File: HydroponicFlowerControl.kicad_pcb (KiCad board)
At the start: 4 copper layers, 101 x 101 mm, 236 parts, among them IC1 ADM3260ARSZ-RL7, IC2 ADM3260ARSZ-RL7, IC3 CH224K, J1 EC, J10 Pump 1, J11 Temperature, J12 Pump 2, J13 Pump 3, J14 D IN1, J15 D IN2, J16 D IN3, J17 CAN, J18 Raspberry_Pi_2_3, J19 Conn_ARM_JTAG_SWD_10, J2 Temp, J20 Conn_ARM_JTAG_SWD_10, J3 Flow, J4 pH, J5 USB_C_Receptacle_USB2.0, J6 Barrel_Jack, J7 Valve 1, J8 Valve 2, J9 Valve 3, Q1 MMBT3904, Q10 AO3401A, Q11 MMBT3904, Q12 AO3401A, Q2 AO3401A, Q3 MMBT3904, Q4 AO3401A, Q5 MMBT3904, Q6 AO3401A, Q7 MMBT3904, Q8 MMBT3904, Q9 AO3401A, SW1 RESET, U1 AT24C256C, U10 REF3020, U11 TPS60400DBV, U12 ADS1115IDGS, U14 TLV271, U15 TLV271, U16 MCP2518FD-xQBB, U17 HDC1080, U18 SN65HVD230, U19 SN65HVD230, U2 ADS1115IDGS, U20 TPS5430DDA, U4 TPS60400DBV, U5 LM324, U6 MCP4017T-502E/LT, U7 LM358, U8 STM32G431CBTx, U9 AMS1117-3.3, Y1 8 MHz, Y2 40MHz

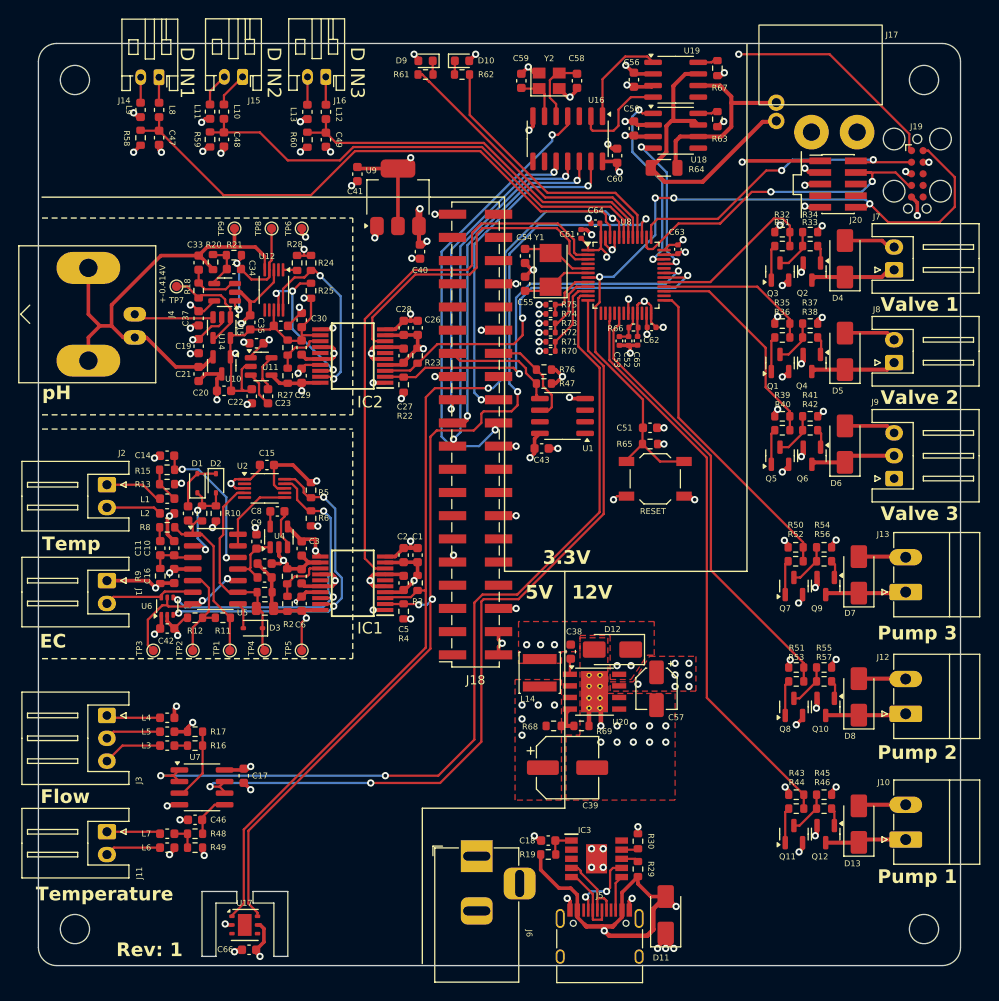
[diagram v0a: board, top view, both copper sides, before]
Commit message: Add testpoints for power and gnd
Closes #3
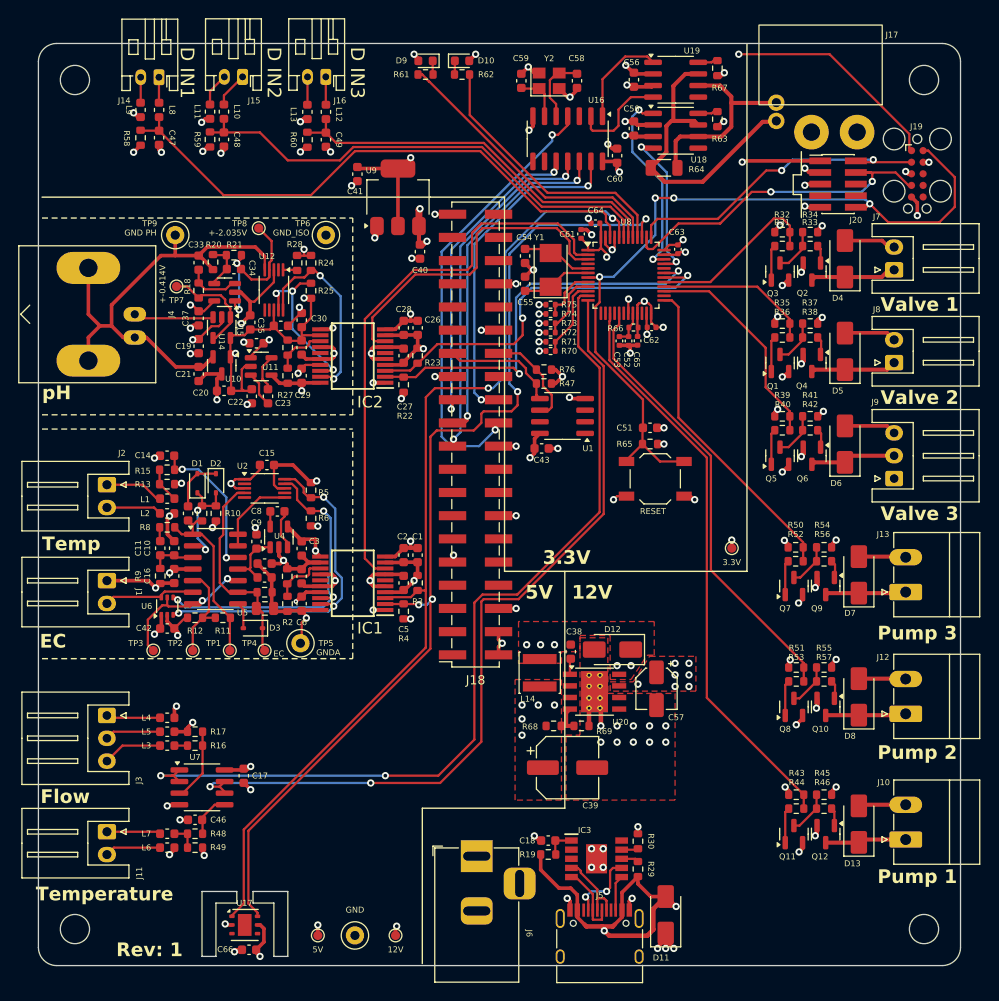
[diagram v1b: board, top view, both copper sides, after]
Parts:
- added TP10: 5V, TestPoint:TestPoint_Pad_D1.0mm, F.Cu at (88.6, 159.7)
- added TP11: 12V, TestPoint:TestPoint_Pad_D1.0mm, F.Cu at (97.1, 159.7)
- added TP12: 3.3V, TestPoint:TestPoint_Pad_D1.0mm, F.Cu at (133.9, 117.3)
- added TP13: GND, TestPoint:TestPoint_Loop_D1.80mm_Drill1.0mm_Beaded, F.Cu at (92.7, 159.7)
- TP4: value TestPoint_Small -> EC
- TP5: value GND_ISO -> GNDA; footprint TestPoint:TestPoint_Pad_D1.0mm -> TestPoint:TestPoint_Loop_D1.80mm_Drill1.0mm_Beaded
- TP6, TP9: footprint TestPoint:TestPoint_Pad_D1.0mm -> TestPoint:TestPoint_Loop_D1.80mm_Drill1.0mm_Beaded
- moved TP9 6.53 mm to (73.0, 83.0)
- moved TP6 2.75 mm to (89.5, 83.0)
- moved TP8 1.41 mm to (82.1, 82.2)
- moved TP5 0.81 mm to (86.7, 127.7)
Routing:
- net +12V: track 16.9 -> 30.5 mm, vias 22 -> 23
- net +5V: track 36.5 -> 37.7 mm, vias 16 -> 17
- net +3.3V: track 84.6 -> 85.5 mm, vias 21 -> 22
- net GND_iosPH: track 36.8 -> 36.0 mm, vias 11 -> 10
- net GNDA: track 51.8 -> 51.1 mm
- net /pH/PH_OUT: track 17.4 -> 18.0 mm

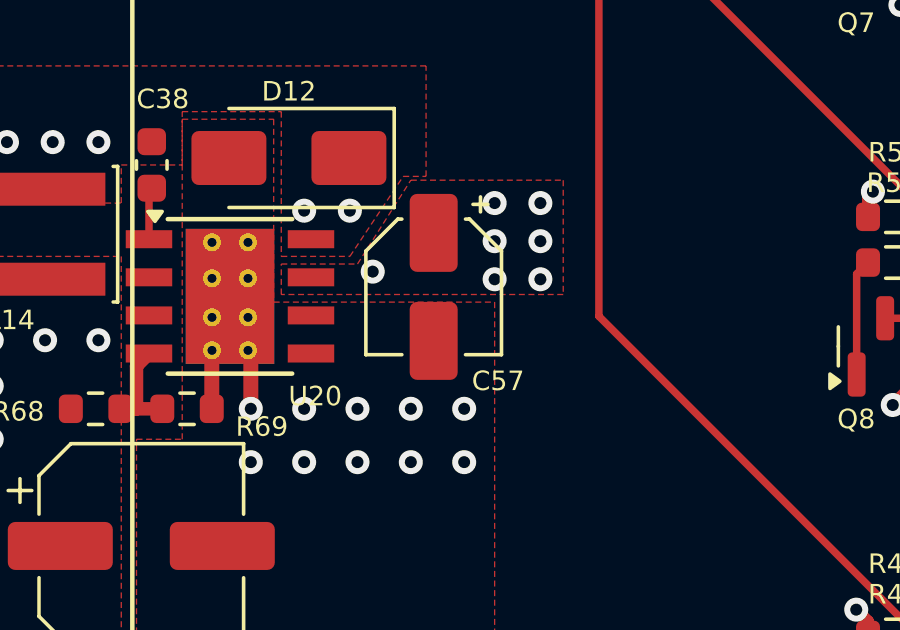
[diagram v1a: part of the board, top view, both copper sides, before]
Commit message: Replace C57
With a variant that can be used with economy pcbs at JLCPCB
Closes #25
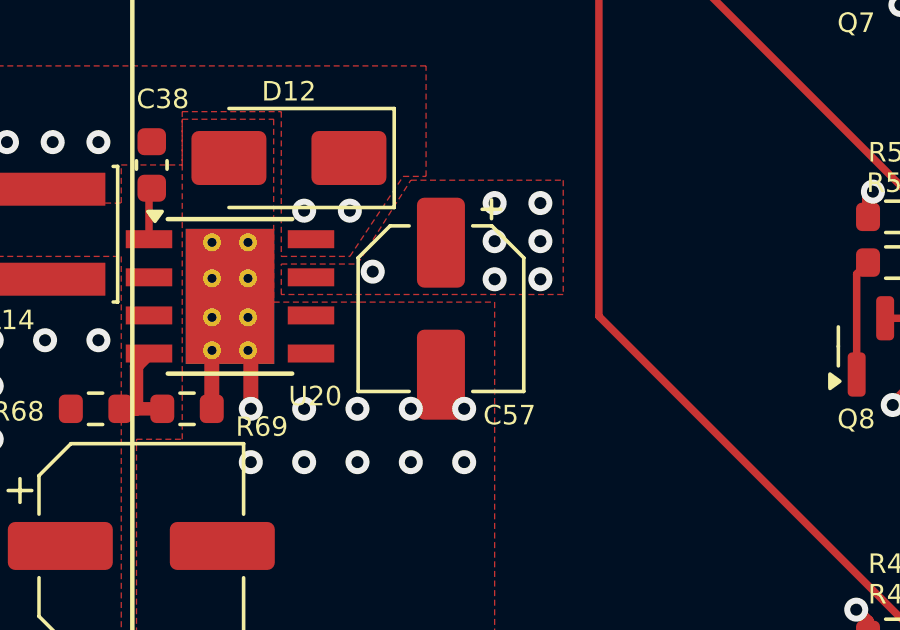
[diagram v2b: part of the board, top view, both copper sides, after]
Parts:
- C57: footprint Capacitor_SMD:CP_Elec_4x5.4 -> Capacitor_SMD:CP_Elec_5x5.4
- moved C57 0.77 mm to (125.9, 133.4)

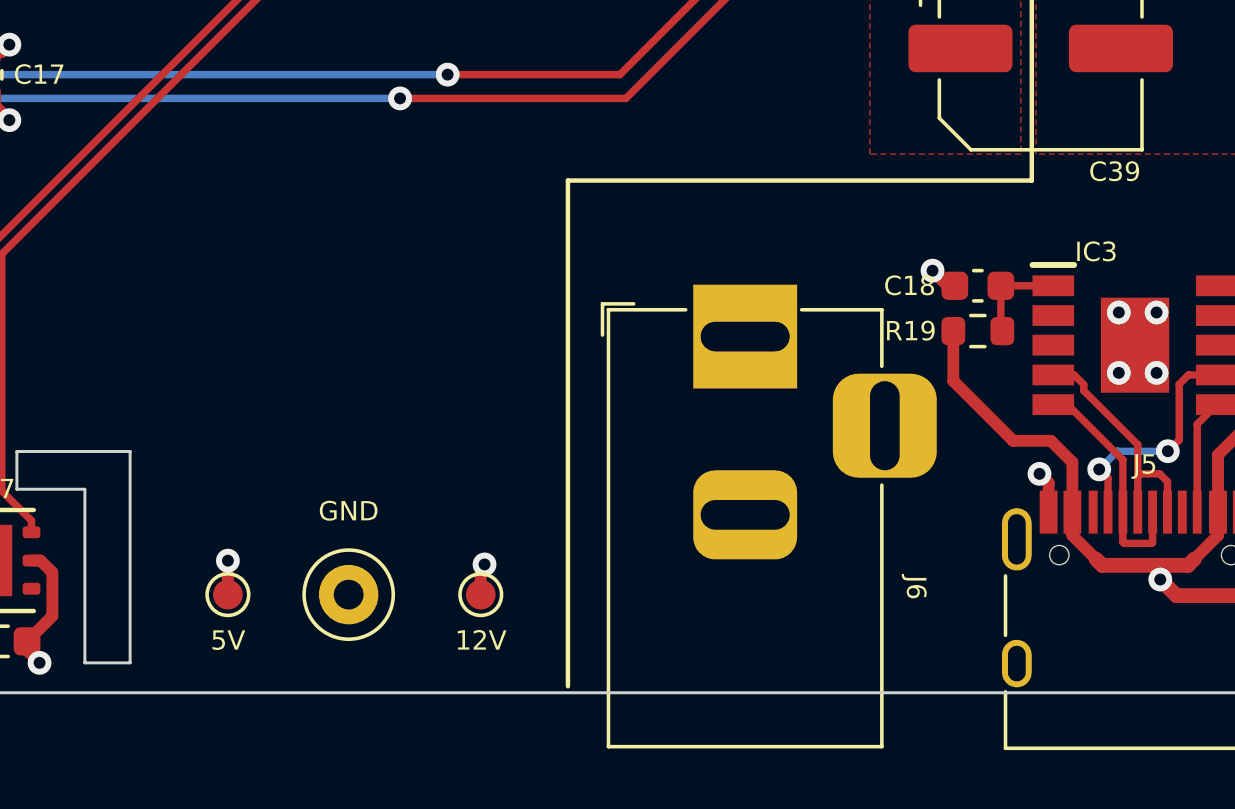
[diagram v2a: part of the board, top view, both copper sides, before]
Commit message: Replace DC connector with SMD variant
Closes #23
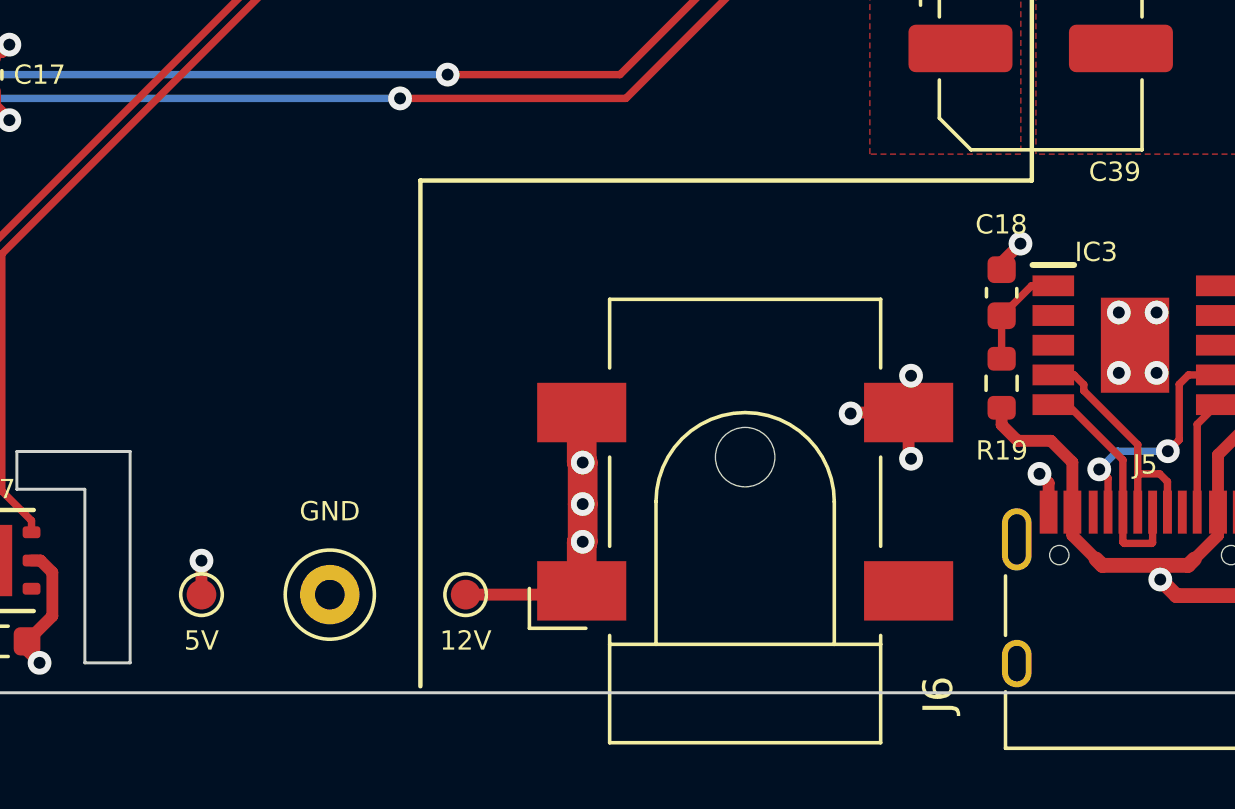
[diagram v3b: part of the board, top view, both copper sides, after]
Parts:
- J6: footprint Connector_BarrelJack:BarrelJack_Horizontal -> Connector_BarrelJack:BarrelJack_CLIFF_FC681465S_SMT_Horizontal
- moved J6 5.56 mm to (106.0, 156.6)
- moved R19 1.93 mm to (114.6, 152.6), turned to -90 degrees
- moved TP10 0.89 mm to (87.7, 159.7)
- moved C18 0.83 mm to (114.6, 149.5), turned to 90 degrees
- moved TP13 0.64 mm to (92.0, 159.7)
- moved TP11 0.51 mm to (96.6, 159.7)
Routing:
- net GND: track 154.4 -> 159.7 mm, vias 90 -> 93
- net +12V: track 30.5 -> 26.7 mm, vias 23 -> 25
- net VBUS: track 45.9 -> 42.6 mm

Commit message: Replace the mcu to a STM32G473 variant
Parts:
- U8: value STM32G431CBTx -> STM32G473CBTx
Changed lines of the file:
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@@
 			)
 		)
-		(property "Value" "STM32G431CBTx"
+		(property "Value" "STM32G473CBTx"
 			(at 0 5.85 0)
 			(layer "F.Fab")
@@
 			)
 		)
-		(property "Datasheet" "https://www.st.com/resource/en/datasheet/stm32g431cb.pdf"
+		(property "Datasheet" "https://www.st.com/resource/en/datasheet/stm32g473cb.pdf"
 			(at 0 0 0)
 			(unlocked yes)
@@
 			)
 		)
-		(property "Description" "STMicroelectronics Arm Cortex-M4 MCU, 128KB flash, 32KB RAM, 170 MHz, 1.71-3.6V, 38 GPIO, LQFP48"
+		(property "Description" "STMicroelectronics Arm Cortex-M4 MCU, 128KB flash, 128KB RAM, 170 MHz, 1.71-3.6V, 38 GPIO, LQFP48"
 			(at 0 0 0)
 			(unlocked yes)
@@
 			)
 		)
-		(property "LCSC" "C529355"
+		(property "LCSC" "C730111"
 			(at 0 0 0)
 			(unlocked yes)
-			(layer "F.Fab")
-			(hide yes)
-			(effects
-				(font
-					(size 1 1)
-					(thickness 0.15)
-				)
-			)
-		)
-		(property "LCSC alt" ""
-			(at 0 0 0)
-			(unlocked yes)

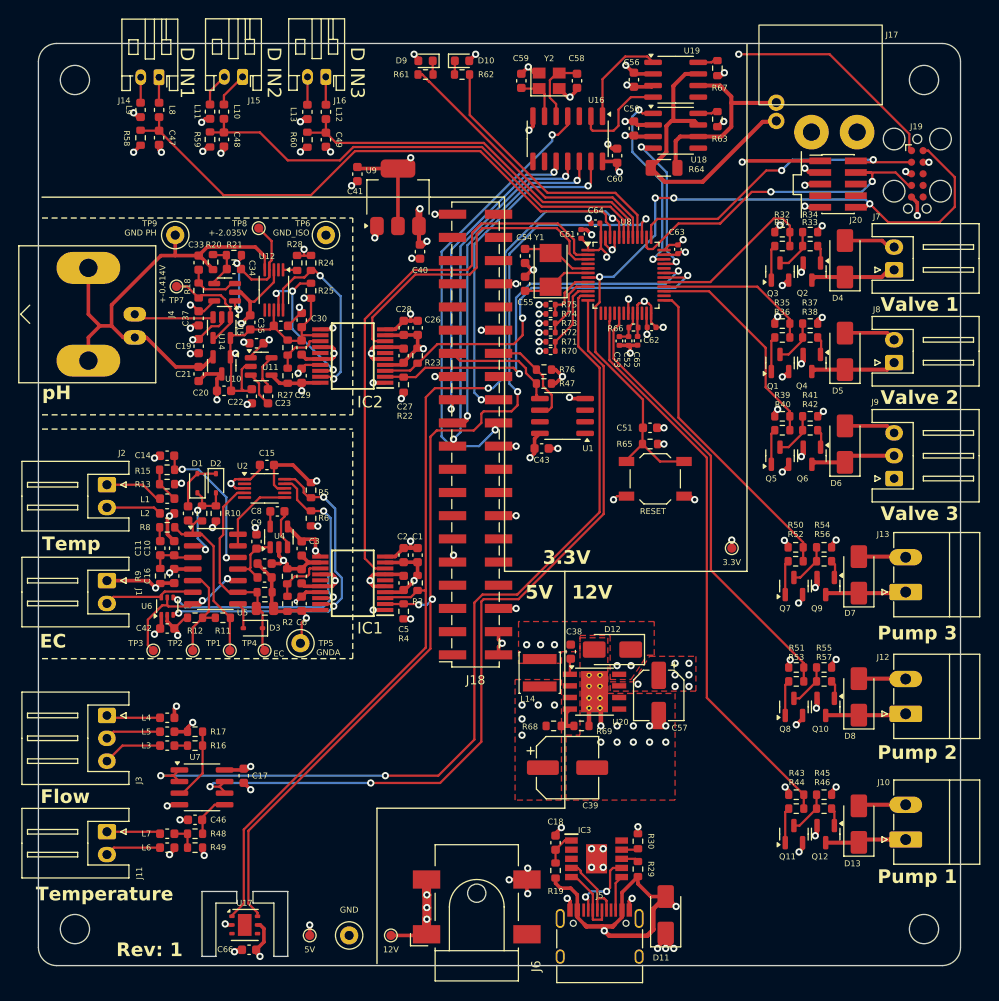
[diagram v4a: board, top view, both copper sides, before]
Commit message: Route USB data signals to STM32
The CANbus needed to be moved together with ec and ph disable signals.
Closes #14 and #9
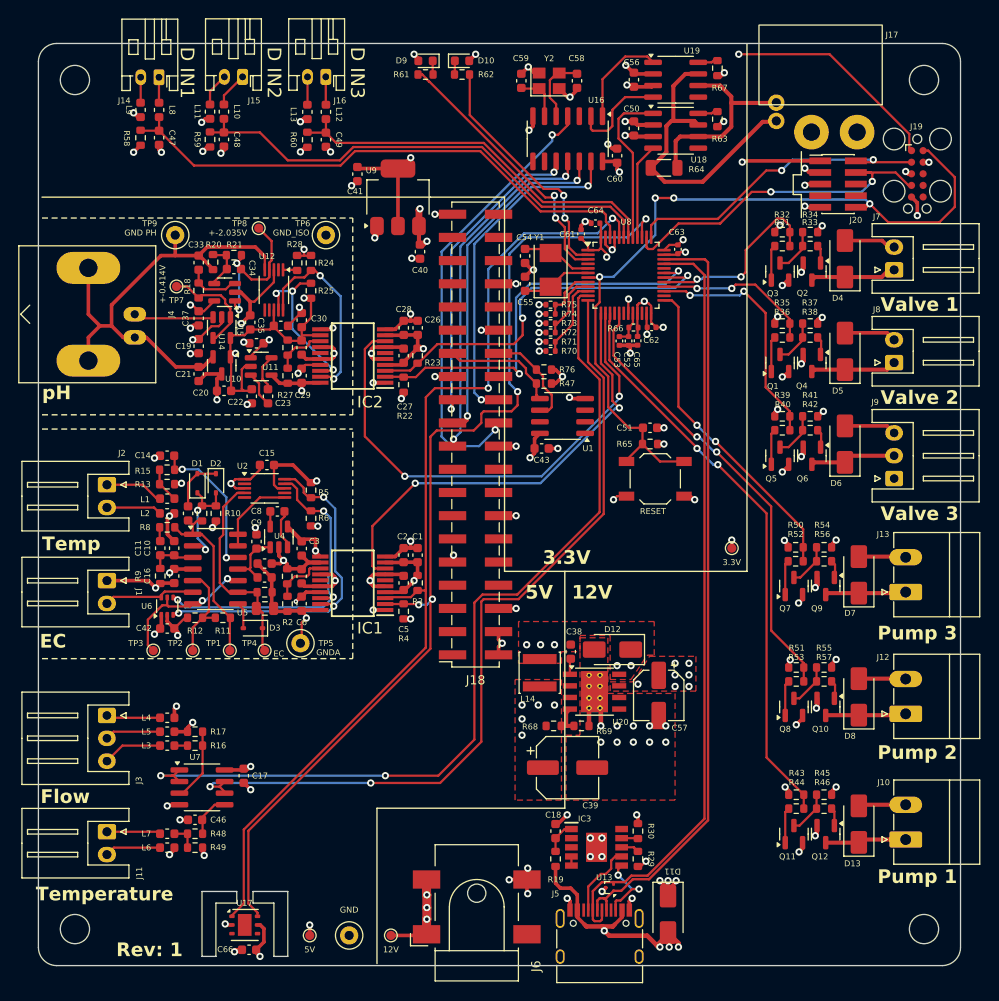
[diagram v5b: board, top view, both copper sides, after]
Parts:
- added U13: TPD2EUSB30, Package_TO_SOT_SMD:Texas_DRT-3, F.Cu at (120.6, 154.5)
- moved C18 1.27 mm to (114.6, 148.3)
- moved R19 1.27 mm to (114.6, 151.3)
- moved IC3 1.26 mm to (119.1, 150.0)
- moved R29 1.11 mm to (123.7, 151.3)
- moved R30 1.11 mm to (123.7, 148.3)
- moved D11 0.26 mm to (127.0, 157.4), turned to -90 degrees
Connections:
- IC3 pad 4: Net-(IC3-DP) -> Net-(IC3-DM)
- J5 pad A6: Net-(IC3-DP) -> /Power/USB_D+
- J5 pad A7: Net-(IC3-DM) -> /Power/USB_D-
- J5 pad B6: Net-(IC3-DP) -> /Power/USB_D+
- J5 pad B7: Net-(IC3-DM) -> /Power/USB_D-
- U8 pad 13: unconnected-(U8-PA5-Pad13) -> /EC/DISABLE
- U8 pad 14: unconnected-(U8-PA6-Pad14) -> /MCU/pH_disable
- U8 pad 2: /EC/DISABLE -> LED_CAN
- U8 pad 3: /MCU/pH_disable -> LED_HB
- U8 pad 33: CAN_RXD -> /Power/USB_D-
- U8 pad 34: CAN_TXD -> /Power/USB_D+
- U8 pad 40: LED_CAN -> CAN_RXD
- U8 pad 41: LED_HB -> CAN_TXD
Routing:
- net /Power/USB_D-: track 0.00 -> 85.5 mm
- net /Power/USB_D+: track 0.00 -> 84.3 mm
- net /MCU/pH_disable: track 35.9 -> 55.3 mm, vias 0 -> 2
- net /EC/DISABLE: track 62.0 -> 49.5 mm, vias 0 -> 2
- net Net-(IC3-DP): track 8.34 -> 0.00 mm
- net Net-(IC3-DM): track 7.45 -> 1.00 mm
- net CAN_RXD: track 16.7 -> 10.5 mm, vias 2 -> 0
- net /Power/CC2: track 3.89 -> 8.21 mm, vias 0 -> 2
- net VBUS: track 42.6 -> 46.7 mm, vias 2 -> 5
- net CAN_TXD: track 21.3 -> 17.7 mm, vias 2 -> 0
- net LED_CAN: track 29.8 -> 26.8 mm, vias 0 -> 2
- net /IO/D_IN1: track 62.9 -> 60.2 mm
- net /Flow control/Valve3: track 23.8 -> 26.4 mm, vias 0 -> 2
- net LED_HB: track 32.2 -> 30.0 mm, vias 0 -> 2
- net /Flow control/Valve1: track 19.2 -> 20.6 mm, vias 0 -> 2
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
